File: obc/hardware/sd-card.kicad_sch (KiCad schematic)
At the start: 7 parts, among them J2 Micro_SD_Card

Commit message: add RTC battery and sensors, preliminary layout
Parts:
- C22: footprint (none) -> Capacitor_SMD:C_0603_1608Metric
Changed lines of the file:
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@@
 			)
 		)
-		(property "Footprint" ""
+		(property "Footprint" "Capacitor_SMD:C_0603_1608Metric"
 			(at 129.54 49.53 0)
 			(hide yes)

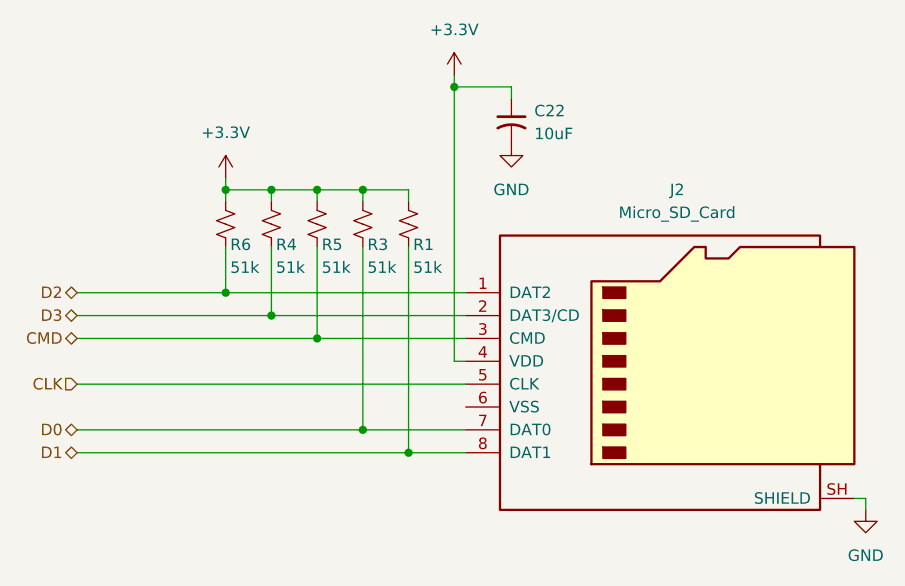
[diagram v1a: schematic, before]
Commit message: added CAN, UART, supervisor, USB, power OR-ing, GPS, did layout
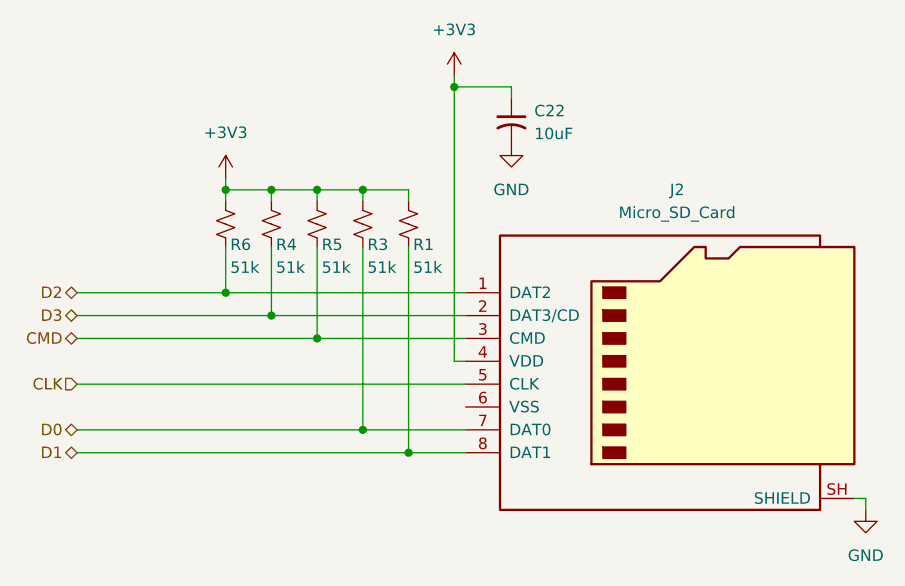
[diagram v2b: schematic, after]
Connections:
- net +3.3V renamed +3V3
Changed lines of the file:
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@@
 	)
 	(symbol
-		(lib_id "power:+3.3V")
+		(lib_id "power:+3V3")
 		(at 123.19 44.45 0)
 		(unit 1)
@@
 		(dnp no)
 		(fields_autoplaced yes)
-		(property "Reference" "#PWR019"
+		(property "Reference" "#PWR19"
 			(at 123.19 48.26 0)
 			(hide yes)
@@
 			)
 		)
-		(property "Value" "+3.3V"
+		(property "Value" "+3V3"
 			(at 123.19 39.37 0)
 			(show_name no)
@@
 			)
 		)
-		(property "Description" "Power symbol creates a global label with name \"+3.3V\""
+		(property "Description" "Power symbol creates a global label with name \"+3V3\""
 			(at 123.19 44.45 0)
 			(hide yes)
@@
 			(project "obc"
 				(path "/ba4f88ff-24aa-49a3-8871-8c7e48b371c5/75414032-b1b6-4f30-95af-cd55b9adc71e/4fcb8da8-6e92-4635-9bd0-4111fcfef293"
-					(reference "#PWR019")
+					(reference "#PWR19")
 					(unit 1)
 				)
@@
 	)
 	(symbol
-		(lib_id "power:+3.3V")
+		(lib_id "power:+3V3")
 		(at 97.79 55.88 0)
 		(unit 1)
@@
 		(dnp no)
 		(fields_autoplaced yes)
-		(property "Reference" "#PWR018"
+		(property "Reference" "#PWR18"
 			(at 97.79 59.69 0)
 			(hide yes)
@@
 			)
 		)
-		(property "Value" "+3.3V"
+		(property "Value" "+3V3"
 			(at 97.79 50.8 0)
 			(show_name no)
@@
 			)
 		)
-		(property "Description" "Power symbol creates a global label with name \"+3.3V\""
+		(property "Description" "Power symbol creates a global label with name \"+3V3\""
 			(at 97.79 55.88 0)
 			(hide yes)
@@
 			(project "obc"
 				(path "/ba4f88ff-24aa-49a3-8871-8c7e48b371c5/75414032-b1b6-4f30-95af-cd55b9adc71e/4fcb8da8-6e92-4635-9bd0-4111fcfef293"
-					(reference "#PWR018")
+					(reference "#PWR18")
 					(unit 1)
 				)

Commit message: add antenna supervisor, ESD, reroute some stuff
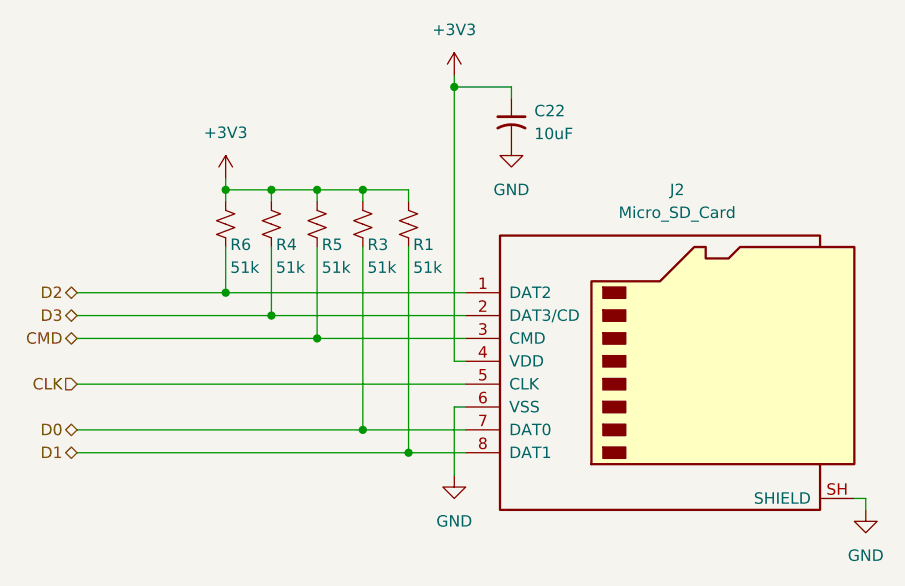
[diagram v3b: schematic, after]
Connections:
- net GND: now also J2.6 (VSS)
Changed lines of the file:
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@@
+	(wire
+		(pts
+			(xy 123.19 81.28) (xy 123.19 88.9)
+		)
+		(stroke
+			(width 0)
+			(type default)
+		)
+	)
 	(wire
 		(pts
@@
 		(pts
 			(xy 113.03 57.15) (xy 107.95 57.15)
+		)
+		(stroke
+			(width 0)
+			(type default)
+		)
+	)
+	(wire
+		(pts
+			(xy 124.46 81.28) (xy 123.19 81.28)
 		)
 		(stroke
@@
 					(unit 1)
 				)
+			)
+		)
+	)
+	(symbol
+		(lib_id "power:GND")
+		(at 123.19 88.9 0)
+		(unit 1)
+		(body_style 1)
+		(exclude_from_sim no)
+		(in_bom yes)
+		(on_board yes)
+		(in_pos_files yes)
+		(dnp no)
+		(fields_autoplaced yes)
+		(property "Reference" "#PWR080"
+			(at 123.19 95.25 0)
+			(hide yes)
+			(show_name no)
+			(do_not_autoplace no)
+			(effects
+				(font
+					(size 1.27 1.27)
+				)
+			)
+		)
+		(property "Value" "GND"
+			(at 123.19 93.98 0)
+			(show_name no)
+			(do_not_autoplace no)
+			(effects
+				(font
+					(size 1.27 1.27)
+				)
+			)
+		)
+		(property "Footprint" ""
+			(at 123.19 88.9 0)
+			(hide yes)
+			(show_name no)
+			(do_not_autoplace no)
+			(effects
+				(font
+					(size 1.27 1.27)
+				)
+			)
+		)
+		(property "Datasheet" ""
+			(at 123.19 88.9 0)
+			(hide yes)
+			(show_name no)
+			(do_not_autoplace no)
+			(effects
+				(font
+					(size 1.27 1.27)
+				)
+			)
+		)
+		(property "Description" "Power symbol creates a global label with name \"GND\" , ground"
+			(at 123.19 88.9 0)
+			(hide yes)
+			(show_name no)
+			(do_not_autoplace no)
+			(effects
+				(font
+					(size 1.27 1.27)
+				)
+			)
+		)
+		(pin "1"
+		)
+		(instances
+			(project "obc"
+				(path "/ba4f88ff-24aa-49a3-8871-8c7e48b371c5/75414032-b1b6-4f30-95af-cd55b9adc71e/4fcb8da8-6e92-4635-9bd0-4111fcfef293"
+					(reference "#PWR080")
+					(unit 1)
+				)

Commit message: cleanup
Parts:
- C22: LCSC (none) -> C19702
- J2: LCSC (none) -> C164170
- R1, R3, R4, R5, R6: LCSC (none) -> C25794
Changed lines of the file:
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@@
+			)
+		)
+		(property "LCSC" "C25794"
+			(at 107.95 60.96 0)
+			(hide yes)
+			(show_name no)
+			(do_not_autoplace no)
+			(effects
+				(font
+					(size 1.27 1.27)
+				)
+			)
+		)
+		(property "KLC_S3.3" ""
+			(at 107.95 60.96 0)
+			(hide yes)
+			(show_name no)
+			(do_not_autoplace no)
+			(effects
+				(font
+					(size 1.27 1.27)
+				)
+			)
+		)
+		(property "KLC_S4.1" ""
+			(at 107.95 60.96 0)
+			(hide yes)
+			(show_name no)
+			(do_not_autoplace no)
+			(effects
+				(font
+					(size 1.27 1.27)
+				)
 			)
 		)
@@
 			)
 		)
+		(property "LCSC" "C25794"
+			(at 97.79 60.96 0)
+			(hide yes)
+			(show_name no)
+			(do_not_autoplace no)
+			(effects
+				(font
+					(size 1.27 1.27)
+				)
+			)
+		)
+		(property "KLC_S3.3" ""
+			(at 97.79 60.96 0)
+			(hide yes)
+			(show_name no)
+			(do_not_autoplace no)
+			(effects
+				(font
+					(size 1.27 1.27)
+				)
+			)
+		)
+		(property "KLC_S4.1" ""
+			(at 97.79 60.96 0)
+			(hide yes)
+			(show_name no)
+			(do_not_autoplace no)
+			(effects
+				(font
+					(size 1.27 1.27)
+				)
+			)
+		)
 		(pin "2"
 		)
@@
 			)
 		)
+		(property "LCSC" "C25794"
+			(at 118.11 60.96 0)
+			(hide yes)
+			(show_name no)
+			(do_not_autoplace no)
+			(effects
+				(font
+					(size 1.27 1.27)
+				)
+			)
+		)
+		(property "KLC_S3.3" ""
+			(at 118.11 60.96 0)
+			(hide yes)
+			(show_name no)
+			(do_not_autoplace no)
+			(effects
+				(font
+					(size 1.27 1.27)
+				)
+			)
+		)
+		(property "KLC_S4.1" ""
+			(at 118.11 60.96 0)
+			(hide yes)
+			(show_name no)
+			(do_not_autoplace no)
+			(effects
+				(font
+					(size 1.27 1.27)
+				)
+			)
+		)
 		(pin "2"
 		)
@@
 			)
 		)
+		(property "LCSC" "C25794"
+			(at 102.87 60.96 0)
+			(hide yes)
+			(show_name no)
+			(do_not_autoplace no)
+			(effects
+				(font
+					(size 1.27 1.27)
+				)
+			)
+		)
+		(property "KLC_S3.3" ""
+			(at 102.87 60.96 0)
+			(hide yes)
+			(show_name no)
+			(do_not_autoplace no)
+			(effects
+				(font
+					(size 1.27 1.27)
+				)
+			)
+		)
+		(property "KLC_S4.1" ""
+			(at 102.87 60.96 0)
+			(hide yes)
+			(show_name no)
+			(do_not_autoplace no)
+			(effects
+				(font
+					(size 1.27 1.27)
+				)
+			)
+		)
 		(pin "2"
 		)
@@
 		)
 		(property "Description" "Resistor, small US symbol"
+			(at 113.03 60.96 0)
+			(hide yes)
+			(show_name no)
+			(do_not_autoplace no)
+			(effects
+				(font
+					(size 1.27 1.27)
+				)
+			)
+		)
+		(property "LCSC" "C25794"
+			(at 113.03 60.96 0)
+			(hide yes)
+			(show_name no)
+			(do_not_autoplace no)
+			(effects
+				(font
+					(size 1.27 1.27)
+				)
+			)
+		)
+		(property "KLC_S3.3" ""
+			(at 113.03 60.96 0)
+			(hide yes)
+			(show_name no)
+			(do_not_autoplace no)
+			(effects
+				(font
+					(size 1.27 1.27)
+				)
+			)
+		)
+		(property "KLC_S4.1" ""
 			(at 113.03 60.96 0)
 			(hide yes)
@@
 			)
 		)
+		(property "LCSC" "C19702"
+			(at 129.54 49.53 0)
+			(hide yes)
+			(show_name no)
+			(do_not_autoplace no)
+			(effects
+				(font
+					(size 1.27 1.27)
+				)
+			)
+		)
+		(property "KLC_S3.3" ""
+			(at 129.54 49.53 0)
+			(hide yes)
+			(show_name no)
+			(do_not_autoplace no)
+			(effects
+				(font
+					(size 1.27 1.27)
+				)
+			)
+		)
+		(property "KLC_S4.1" ""
+			(at 129.54 49.53 0)
+			(hide yes)
+			(show_name no)
+			(do_not_autoplace no)
+			(effects
+				(font
+					(size 1.27 1.27)
+				)
+			)
+		)
 		(pin "2"
 		)
@@
 			(at 147.32 76.2 0)
 			(hide yes)
+			(show_name no)
+			(do_not_autoplace no)
+			(effects
+				(font
+					(size 1.27 1.27)
+				)
+			)
+		)
+		(property "LCSC" "C164170"
+			(at 147.32 76.2 0)
+			(hide yes)
+			(show_name no)
+			(do_not_autoplace no)
+			(effects
+				(font
+					(size 1.27 1.27)
+				)
+			)
+		)
+		(property "KLC_S3.3" ""
+			(at 147.32 76.2 0)
+			(hide yes)
+			(show_name no)
+			(do_not_autoplace no)
+			(effects
+				(font
+					(size 1.27 1.27)
+				)
+			)
+		)
+		(property "KLC_S4.1" ""
+			(at 147.32 76.2 0)
+			(hide yes)
